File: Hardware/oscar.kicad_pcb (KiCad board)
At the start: 4 copper layers, 80 x 110 mm, 50 parts, among them J1 SWD_Header, J10 LCD_Connector, J2 ChannelA_In, J3 ChannelB_In, J4 ChannelC_In, J5 ChA_Buff_Out, J6 ChB_Buff_Out, J7 ChC_Buff_Out, J8 MIDI_In, J9 Eurorack_16_pin_power, SW1 Left_Encoder, SW2 Right_Encoder, SW3 SW_Push, U1 STM32F446RETx, U2 ILI9341_SPI, U3 MCP6004, U4 TL074, U5 LM1117-3.3, Y1 Crystal

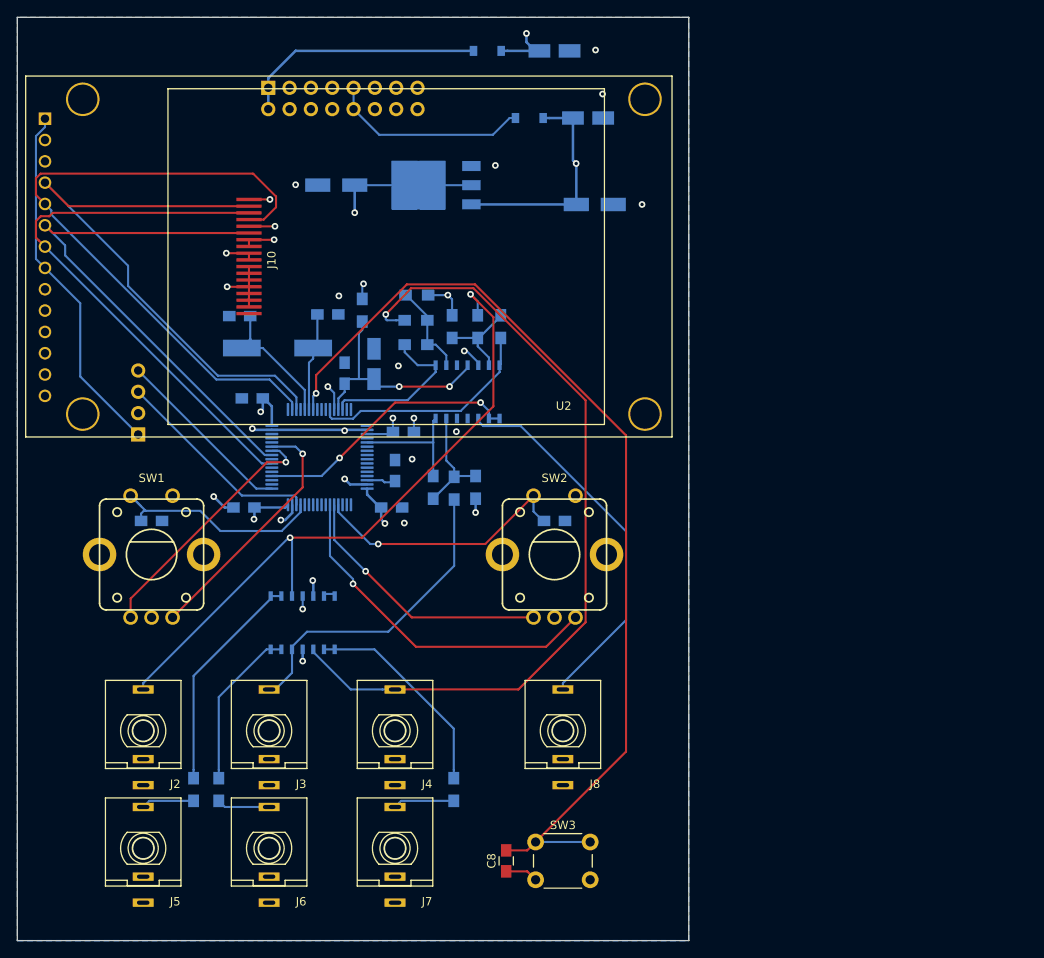
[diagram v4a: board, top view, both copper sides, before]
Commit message: v1 PCB; added zero crossing count config to Circular mode; refactored variables into objects
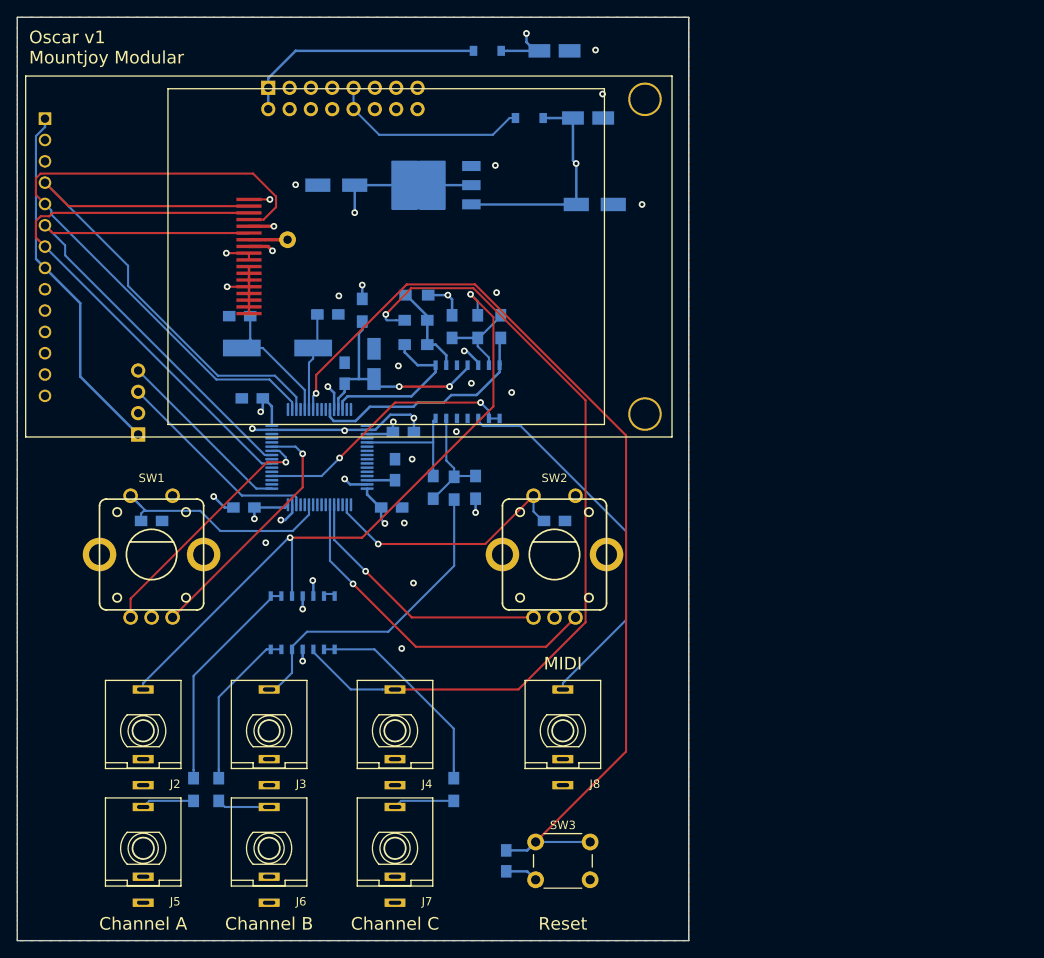
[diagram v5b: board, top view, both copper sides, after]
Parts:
- added J11: MISO_Connector, Wire_Pads:SolderWirePad_single_2mmDrill, F.Cu at (152.8, 74.9)
- C8: moved to B.Cu
- moved C5 0.10 mm to (165.0, 103.9)
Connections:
- net Net-(J2-Pad3) renamed /CHA_In
- net Net-(J3-Pad3) renamed /CHB_In
- net Net-(J4-Pad3) renamed /CHC_In
- net Net-(J5-Pad3) renamed /CHA_Out
- net Net-(J6-Pad3) renamed /CHB_Out
- net Net-(J7-Pad3) renamed /CHC_Out
- net Net-(J8-Pad3) renamed /MIDI_In
- J10 pad 7: GND -> LCD_MISO
- U1 pad 34: Net-(U1-Pad34) -> R_ENC_BTN
- U1 pad 36: R_ENC_BTN -> Net-(U1-Pad36)
- U1 pad 43: Net-(U1-Pad43) -> L_ENC_BTN
- U1 pad 45: L_ENC_BTN -> Net-(U1-Pad45)
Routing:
- net GND: track 52.2 -> 58.5 mm, vias 23 -> 29
- net LCD_MISO: track 0.00 -> 4.60 mm
- net L_ENC_BTN: track 27.1 -> 28.3 mm
- net R_ENC_BTN: track 31.7 -> 30.7 mm
- net +3V3: track 86.6 -> 85.9 mm
- added copper zone on F.Cu, net GND
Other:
- board text added: "+12V"
- board text added: "-12V"
- board text added: "3V3A"
- board text added: "3V3D"
- board text added: "Channel A"
- board text added: "Channel B"
- board text added: "Channel C"
- board text added: "MIDI"
- board text added: "MISO"
- board text added: "Oscar v1 Mountjoy Modular"
- board text added: "Reset"

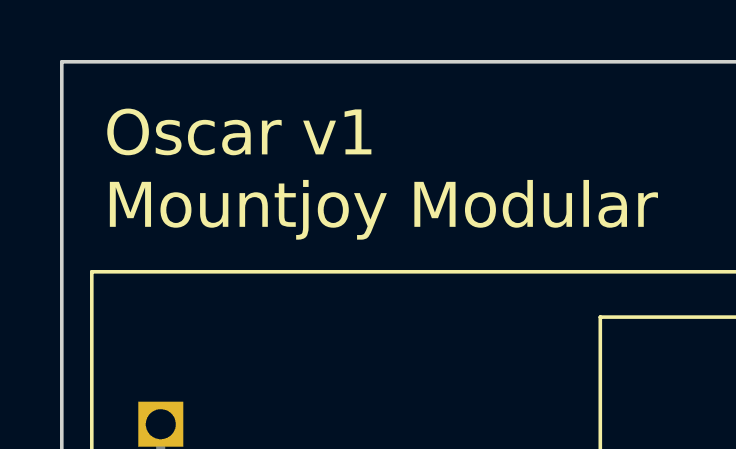
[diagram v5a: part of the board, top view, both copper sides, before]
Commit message: Created LCD daughterboard
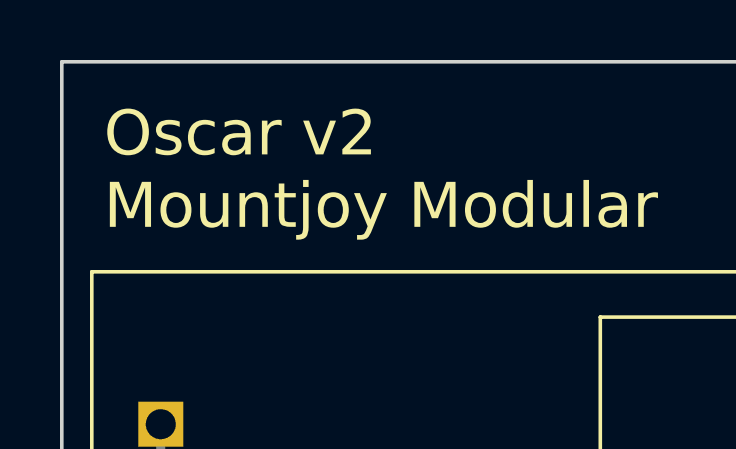
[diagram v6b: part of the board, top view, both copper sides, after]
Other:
- board text added: "3.3V"
- board text added: "Oscar v2 Mountjoy Modular"
- board text removed: "Oscar v1 Mountjoy Modular"
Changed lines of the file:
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@@
   (general
     (thickness 1.6)
-    (drawings 31)
+    (drawings 32)
     (tracks 397)
     (zones 0)
@@
   )
   (setup
-    (last_trace_width 0.3)
+    (last_trace_width 0.25)
     (user_trace_width 0.25)
     (user_trace_width 0.3)
@@
       (effects (font (size 1 1) (thickness 0.15)) (justify mirror))
     )
-    (fp_text value 15k (at -3.75 -2.35) (layer B.SilkS)
+    (fp_text value 15k (at -0.5 3.3) (layer B.SilkS)
       (effects (font (size 1 1) (thickness 0.15)) (justify mirror))
     )
@@
       (effects (font (size 1 1) (thickness 0.15)) (justify mirror))
     )
-    (fp_text value 100k (at 0.775 -5.825 180) (layer B.SilkS)
+    (fp_text value 100k (at 3.9 -1.2 180) (layer B.SilkS)
       (effects (font (size 1 1) (thickness 0.15)) (justify mirror))
     )
@@
       (net 2 GND))
   )
-  (gr_text "Oscar v1\nMountjoy Modular" (at 121.4 53.6) (layer F.SilkS)
+  (gr_text 3.3V (at 127.6 62.2) (layer B.SilkS)
+    (effects (font (size 1 1) (thickness 0.15)) (justify mirror))
+  )
+  (gr_text "Oscar v2\nMountjoy Modular" (at 121.4 53.6) (layer F.SilkS)
     (effects (font (size 1.5 1.5) (thickness 0.3)) (justify left))
   )

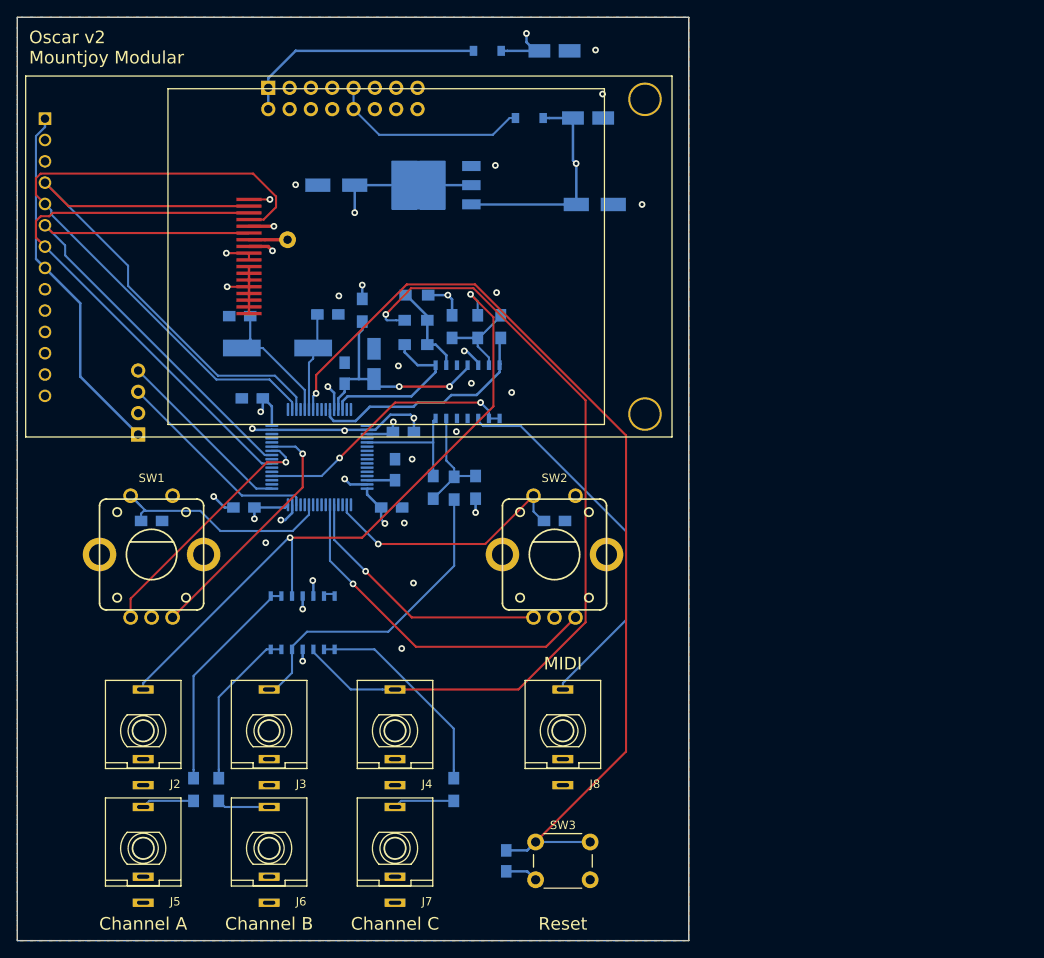
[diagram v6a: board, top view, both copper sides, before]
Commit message: PCB Updated to incorporate LCD daughterboard
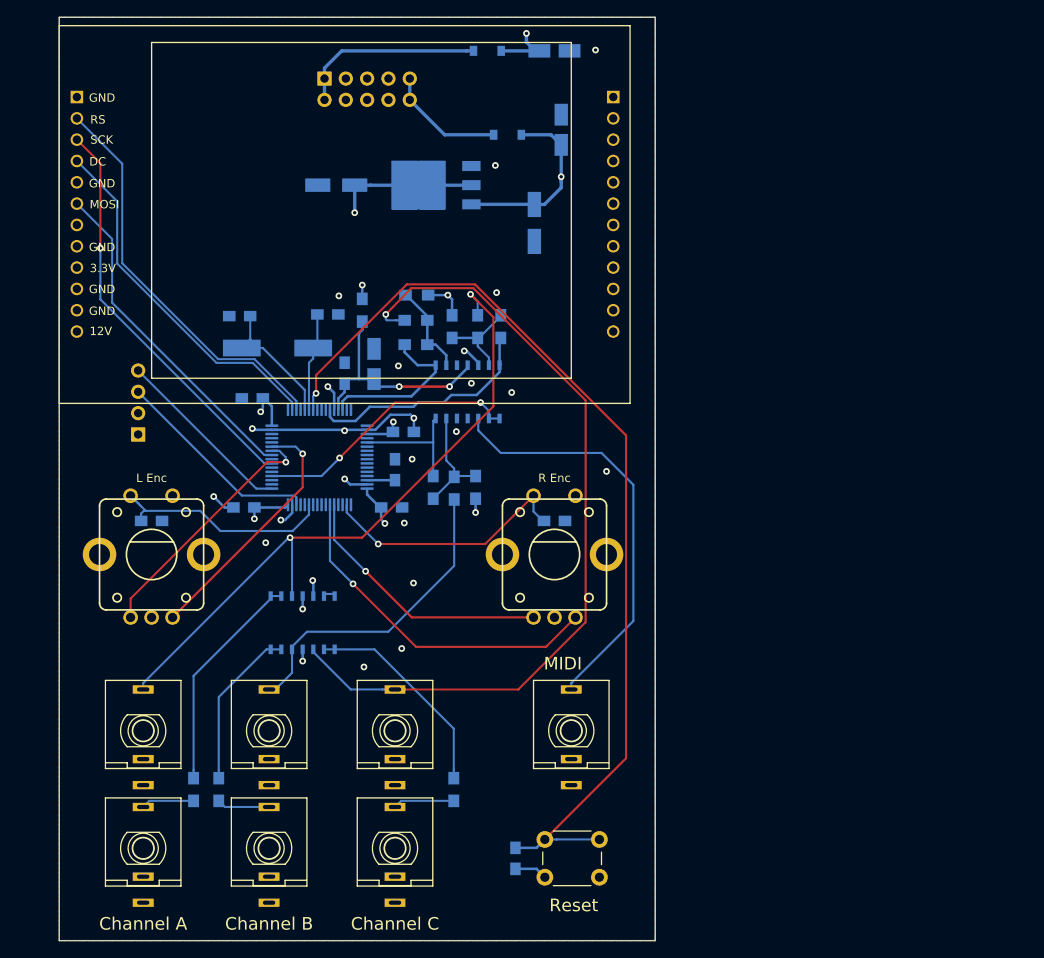
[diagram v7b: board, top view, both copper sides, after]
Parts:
- removed J10: LCD_Connector, Custom_Footprints:18x0.8mmLCDConnector
- removed J11: MISO_Connector, Wire_Pads:SolderWirePad_single_2mmDrill
- J9: value Eurorack_16_pin_power -> Eurorack_10_pin_power; footprint Custom_Footprints:Eurorack_16_pin_header -> Custom_Footprints:Eurorack_10_pin_header
- L Enc: renamed from SW1
- R Enc: renamed from SW2
- U2: value ILI9341_SPI -> ILI9341_SPI_Daughterboard; footprint Custom_Footprints:ILI9341_SPI -> Custom_Footprints:ILI9341_SPI_daughterboard
- moved C11 7.53 mm to (181.6, 74.5), turned to 270 degrees
- moved J9 6.79 mm to (156.6, 57.3)
- moved U2 6.59 mm to (127.1, 59.5)
- moved C12 3.49 mm to (184.8, 63.4), turned to 90 degrees
- moved D1 3.28 mm to (178.4, 64.0)
- moved C8 1.14 mm to (179.3, 150.2)
- moved SW3 1.14 mm to (182.8, 147.9)
- moved J8 1.00 mm to (186.0, 135.0)
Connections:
- U2 pad 1: +3V3 -> GND
- U2 pad 10: Net-(U2-Pad10) -> GND
- U2 pad 11: Net-(U2-Pad11) -> GND
- U2 pad 13: Net-(U2-Pad13) -> GND
- U2 pad 2: GND -> LCD_RESET
- U2 pad 3: GND -> LCD_SCK
- U2 pad 4: LCD_RESET -> LCD_DC
- U2 pad 5: LCD_DC -> GND
- U2 pad 7: LCD_SCK -> Net-(U2-Pad7)
- U2 pad 8: +3V3 -> GND
- U2 pad 9: GND -> +3V3
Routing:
- net +3V3: track 85.9 -> 39.3 mm, vias 7 -> 6
- net LCD_DC: track 79.0 -> 42.7 mm
- net LCD_MOSI: track 63.7 -> 40.1 mm
- net LCD_RESET: track 68.9 -> 48.1 mm
- net LCD_SCK: track 67.0 -> 48.7 mm, vias 0 -> 1
- net GND: track 58.5 -> 41.9 mm, vias 29 -> 24
- net +12V: track 23.9 -> 14.3 mm
- net -12V: track 29.5 -> 22.4 mm
- net /MIDI_In: track 45.3 -> 50.3 mm
- net VCC: track 27.9 -> 23.3 mm
- net LCD_MISO: track 4.60 -> 0.00 mm
- net NRST: track 116.4 -> 115.7 mm
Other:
- board size 80 x 110 mm -> 71 x 110 mm
- board text added: "1"
- board text added: "12V"
- board text added: "17"
- board text added: "33"
- board text added: "49"
- board text added: "DC"
- board text added: "GND"
- board text added: "MOSI"
- board text added: "RS"
- board text added: "SCK"
- board text removed: "MISO"

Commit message: Added panel PCB
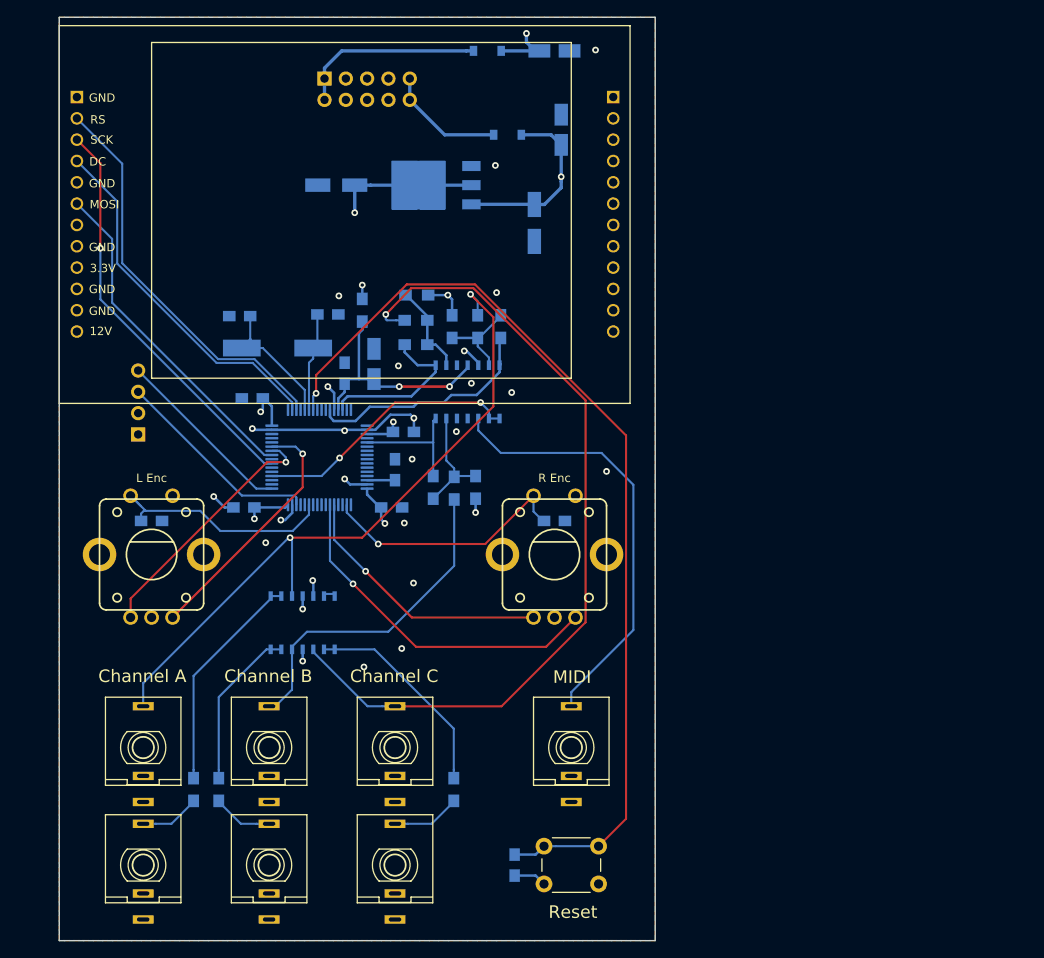
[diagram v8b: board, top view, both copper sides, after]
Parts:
- moved J2 2.00 mm to (135.0, 137.0)
- moved J3 2.00 mm to (150.0, 137.0)
- moved J4 2.00 mm to (165.0, 137.0)
- moved J5 2.00 mm to (135.0, 151.0)
- moved J6 2.00 mm to (150.0, 151.0)
- moved J7 2.00 mm to (165.0, 151.0)
- moved J8 2.00 mm to (186.0, 137.0)
- moved C8 0.81 mm to (179.2, 151.0)
- moved SW3 0.81 mm to (182.8, 148.8)
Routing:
- net /CHB_In: track 38.0 -> 40.0 mm
- net /CHA_In: track 80.9 -> 82.9 mm
- net /MIDI_In: track 50.3 -> 52.3 mm
- net NRST: track 115.7 -> 113.8 mm
- net /CHC_In: track 97.9 -> 99.5 mm
- net /CHC_Out: track 7.30 -> 8.19 mm
- net /CHB_Out: track 6.30 -> 7.19 mm
- net /CHA_Out: track 6.30 -> 7.19 mm
